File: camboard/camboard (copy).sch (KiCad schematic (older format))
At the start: 7 parts

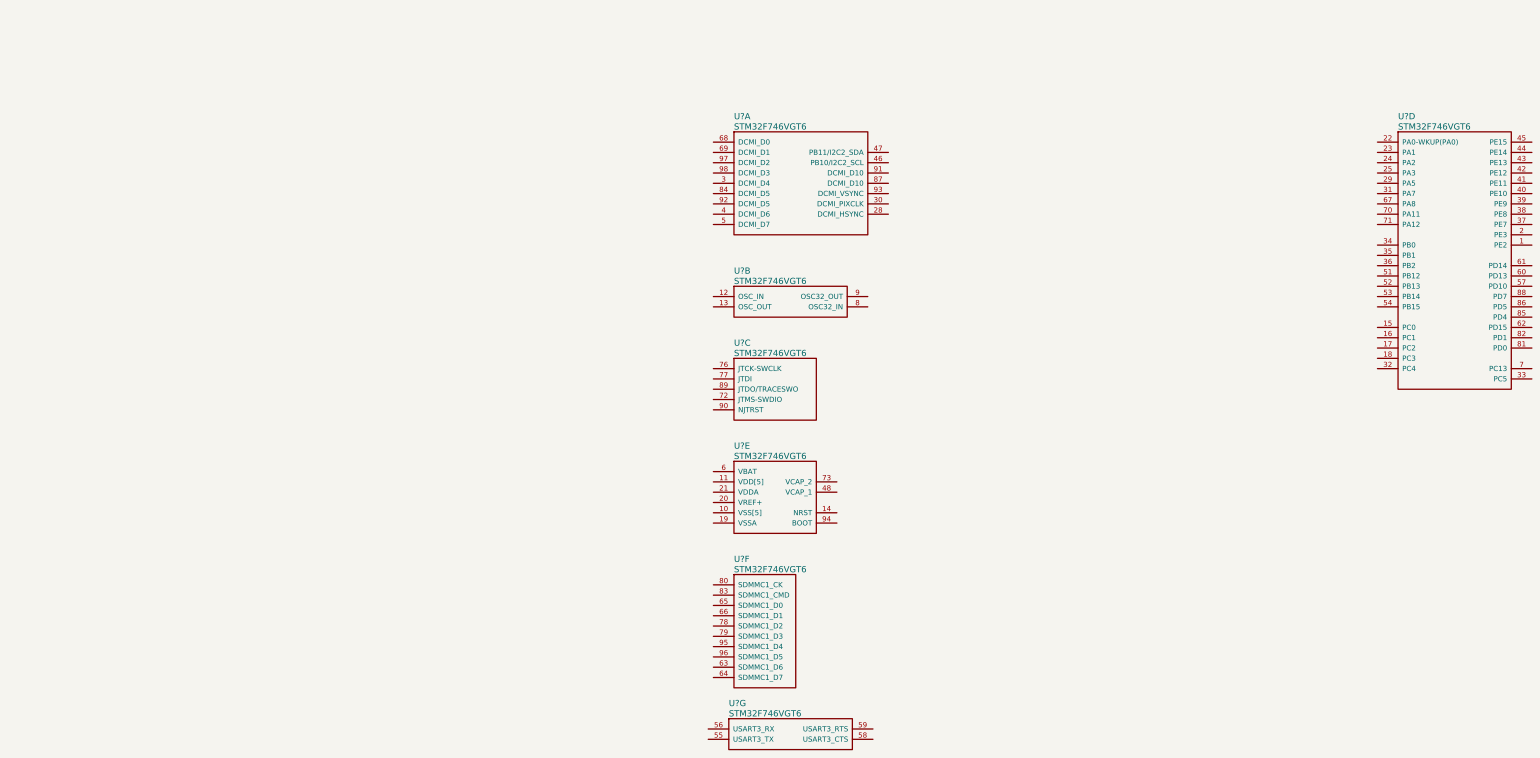
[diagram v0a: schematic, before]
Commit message: Moved components into proper directory
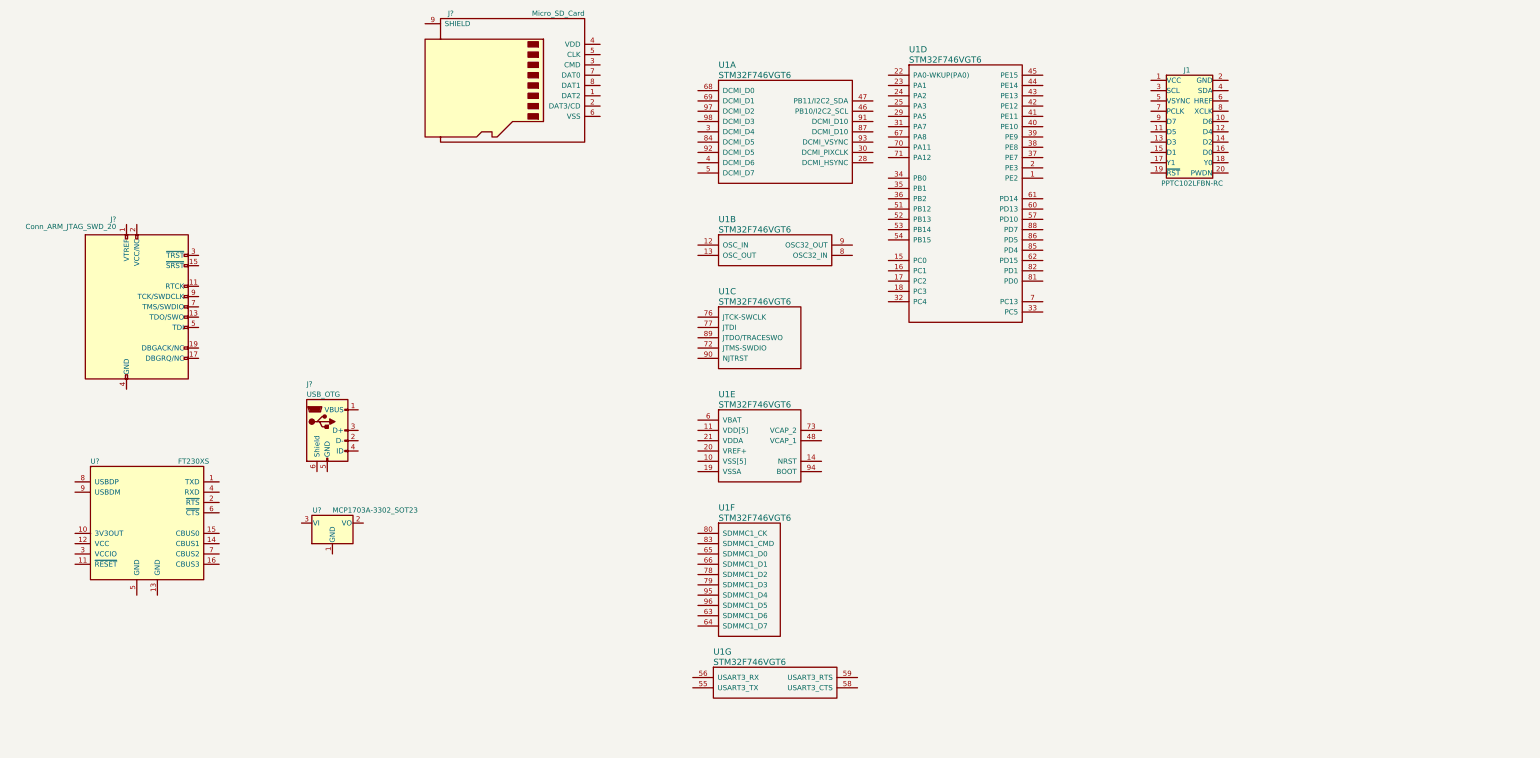
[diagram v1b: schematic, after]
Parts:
- added J1: PPTC102LFBN-RC, symbol PPTC102LFBN-RC
- added J?: Micro_SD_Card, symbol Micro_SD_Card
- added J?: Conn_ARM_JTAG_SWD_20, symbol Conn_ARM_JTAG_SWD_20
- added J?: USB_OTG, symbol USB_OTG
- added U?: FT230XS, SSOP-16, symbol FT230XS
- added U?: MCP1703A-3302_SOT23, TO_SOT_Packages_SMD:SOT-23, symbol MCP1703A-3302_SOT23
- gave numbers to parts that had none: 1
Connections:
- new net GND: J?.10 (GND), J?.12 (GND), J?.14 (GND), J?.16 (GND), J?.18 (GND), J?.20 (GND), J?.4 (GND), J?.6 (GND), J?.8 (GND)
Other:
- moved on the sheet: U1A, U1B, U1C, U1D, U1E, U1F, U1G
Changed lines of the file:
@@
 EESchema Schematic File Version 2
+LIBS:components
+LIBS:connectors
+LIBS:stm32-v2
 LIBS:power
 LIBS:device
@@
 LIBS:contrib
 LIBS:valves
-LIBS:STM32F7x
-LIBS:stm32-v2
-LIBS:camboard-cache
+LIBS:ftdi
+LIBS:camboard (copy)-cache
 EELAYER 25 0
 EELAYER END
@@
 $EndDescr
 $Comp
-L STM32F746VGT6 U?
+L STM32F746VGT6 U1
 U 1 1 59CAFAA7
-P 1300 1750
-F 0 "U?" H 1500 2000 60  0000 L CNN
-F 1 "STM32F746VGT6" H 1500 1900 60  0000 L CNN
-F 2 "" H 1300 1750 60  0001 C CNN
-F 3 "" H 1300 1750 60  0001 C CNN
-	1    1300 1750
+P 1150 1250
+F 0 "U1" H 1350 1500 60  0000 L CNN
+F 1 "STM32F746VGT6" H 1350 1400 60  0000 L CNN
+F 2 "" H 1150 1250 60  0001 C CNN
+F 3 "" H 1150 1250 60  0001 C CNN
+	1    1150 1250
 	1    0    0    -1
 $EndComp
 $Comp
-L STM32F746VGT6 U?
+L STM32F746VGT6 U1
 U 2 1 59CAFB26
-P 1300 3250
-F 0 "U?" H 1500 3500 60  0000 L CNN
-F 1 "STM32F746VGT6" H 1500 3400 60  0000 L CNN
-F 2 "" H 1300 3250 60  0001 C CNN
-F 3 "" H 1300 3250 60  0001 C CNN
-	2    1300 3250
+P 1150 2750
+F 0 "U1" H 1350 3000 60  0000 L CNN
+F 1 "STM32F746VGT6" H 1350 2900 60  0000 L CNN
+F 2 "" H 1150 2750 60  0001 C CNN
+F 3 "" H 1150 2750 60  0001 C CNN
+	2    1150 2750
 	1    0    0    -1
 $EndComp
 $Comp
-L STM32F746VGT6 U?
+L STM32F746VGT6 U1
 U 3 1 59CAFB7D
-P 1300 3950
-F 0 "U?" H 1500 4200 60  0000 L CNN
-F 1 "STM32F746VGT6" H 1500 4100 60  0000 L CNN
-F 2 "" H 1300 3950 60  0001 C CNN
-F 3 "" H 1300 3950 60  0001 C CNN
-	3    1300 3950
+P 1150 3450
+F 0 "U1" H 1350 3700 60  0000 L CNN
+F 1 "STM32F746VGT6" H 1350 3600 60  0000 L CNN
+F 2 "" H 1150 3450 60  0001 C CNN
+F 3 "" H 1150 3450 60  0001 C CNN
+	3    1150 3450
 	1    0    0    -1
 $EndComp
 $Comp
-L STM32F746VGT6 U?
+L STM32F746VGT6 U1
 U 4 1 59CAFBB8
-P 7750 1750
-F 0 "U?" H 7950 2000 60  0000 L CNN
-F 1 "STM32F746VGT6" H 7950 1900 60  0000 L CNN
-F 2 "" H 7750 1750 60  0001 C CNN
-F 3 "" H 7750 1750 60  0001 C CNN
-	4    7750 1750
+P 3000 1100
+F 0 "U1" H 3200 1350 60  0000 L CNN
+F 1 "STM32F746VGT6" H 3200 1250 60  0000 L CNN
+F 2 "" H 3000 1100 60  0001 C CNN
+F 3 "" H 3000 1100 60  0001 C CNN
+	4    3000 1100
 	1    0    0    -1
 $EndComp
 $Comp
-L STM32F746VGT6 U?
+L STM32F746VGT6 U1
 U 5 1 59CAFC81
-P 1300 4950
-F 0 "U?" H 1500 5200 60  0000 L CNN
-F 1 "STM32F746VGT6" H 1500 5100 60  0000 L CNN
-F 2 "" H 1300 4950 60  0001 C CNN
-F 3 "" H 1300 4950 60  0001 C CNN
-	5    1300 4950
+P 1150 4450
+F 0 "U1" H 1350 4700 60  0000 L CNN
+F 1 "STM32F746VGT6" H 1350 4600 60  0000 L CNN
+F 2 "" H 1150 4450 60  0001 C CNN
+F 3 "" H 1150 4450 60  0001 C CNN
+	5    1150 4450
 	1    0    0    -1
 $EndComp
 $Comp
-L STM32F746VGT6 U?
+L STM32F746VGT6 U1
 U 6 1 59CAFD02
-P 1300 6050
-F 0 "U?" H 1500 6300 60  0000 L CNN
-F 1 "STM32F746VGT6" H 1500 6200 60  0000 L CNN
-F 2 "" H 1300 6050 60  0001 C CNN
-F 3 "" H 1300 6050 60  0001 C CNN
-	6    1300 6050
+P 1150 5550
+F 0 "U1" H 1350 5800 60  0000 L CNN
+F 1 "STM32F746VGT6" H 1350 5700 60  0000 L CNN
+F 2 "" H 1150 5550 60  0001 C CNN
+F 3 "" H 1150 5550 60  0001 C CNN
+	6    1150 5550
 	1    0    0    -1
 $EndComp
 $Comp
-L STM32F746VGT6 U?
+L STM32F746VGT6 U1
 U 7 1 59CAFE6F
-P 1250 7450
-F 0 "U?" H 1450 7700 60  0000 L CNN
-F 1 "STM32F746VGT6" H 1450 7600 60  0000 L CNN
-F 2 "" H 1250 7450 60  0001 C CNN
-F 3 "" H 1250 7450 60  0001 C CNN
-	7    1250 7450
+P 1100 6950
+F 0 "U1" H 1300 7200 60  0000 L CNN
+F 1 "STM32F746VGT6" H 1300 7100 60  0000 L CNN
+F 2 "" H 1100 6950 60  0001 C CNN
+F 3 "" H 1100 6950 60  0001 C CNN
+	7    1100 6950
 	1    0    0    -1
 $EndComp
+$Comp
+L PPTC102LFBN-RC J1
+U 1 1 59CBC2A2
+P 5750 1550
+F 0 "J1" H 5900 2050 50  0000 C CNN
+F 1 "PPTC102LFBN-RC" H 5950 950 50  0000 C CNN
+F 2 "" H 4400 1400 50  0001 C CNN
+F 3 "" H 6050 2050 50  0001 C CNN
+	1    5750 1550
+	1    0    0    -1
+$EndComp
+$Comp
+L Micro_SD_Card J?
+U 1 1 59CBC7CA
+P -600 1100
+F 0 "J?" H -1250 1700 50  0000 C CNN
+F 1 "Micro_SD_Card" H 50  1700 50  0000 R CNN
+F 2 "" H 550 1400 50  0001 C CNN
+F 3 "" H -600 1100 50  0001 C CNN
+	1    -600 1100
+	1    0    0    -1
+$EndComp
+$Comp
+L Conn_ARM_JTAG_SWD_20 J?
+U 1 1 59CBC9BD
+P -4300 3350
+F 0 "J?" H -4500 4200 50  0000 R CNN
+F 1 "Conn_ARM_JTAG_SWD_20" H -4500 4100 50  0000 R BNN
+F 2 "" H -3850 2300 50  0001 L TNN
+F 3 "" V -4650 2100 50  0001 C CNN
+	1    -4300 3350
+	1    0    0    -1
+$EndComp
+$Comp
+L FT230XS U?
+U 1 1 59CBCC25
+P -4200 5450
+F 0 "U?" H -4750 6050 50  0000 L CNN
+F 1 "FT230XS" H -3900 6050 50  0000 L CNN
+F 2 "SSOP-16" H -4200 5450 50  0001 C CNN
+F 3 "" H -4200 5450 50  0001 C CNN
+	1    -4200 5450
+	1    0    0    -1
+$EndComp
+$Comp
+L USB_OTG J?
+U 1 1 59CBCF26
+P -2450 4550
+F 0 "J?" H -2650 5000 50  0000 L CNN
+F 1 "USB_OTG" H -2650 4900 50  0000 L CNN
+F 2 "" H -2300 4500 50  0001 C CNN
+F 3 "" H -2300 4500 50  0001 C CNN
+	1    -2450 4550
+	1    0    0    -1
+$EndComp
+$Comp
+L MCP1703A-3302_SOT23 U?
+U 1 1 59CBCF8D
+P -2400 5450
+F 0 "U?" H -2550 5575 50  0000 C CNN
+F 1 "MCP1703A-3302_SOT23" H -2400 5575 50  0000 L CNN
+F 2 "TO_SOT_Packages_SMD:SOT-23" H -2400 5650 50  0001 C CNN
+F 3 "" H -2400 5400 50  0001 C CNN
+	1    -2400 5450
+	1    0    0    -1
+$EndComp

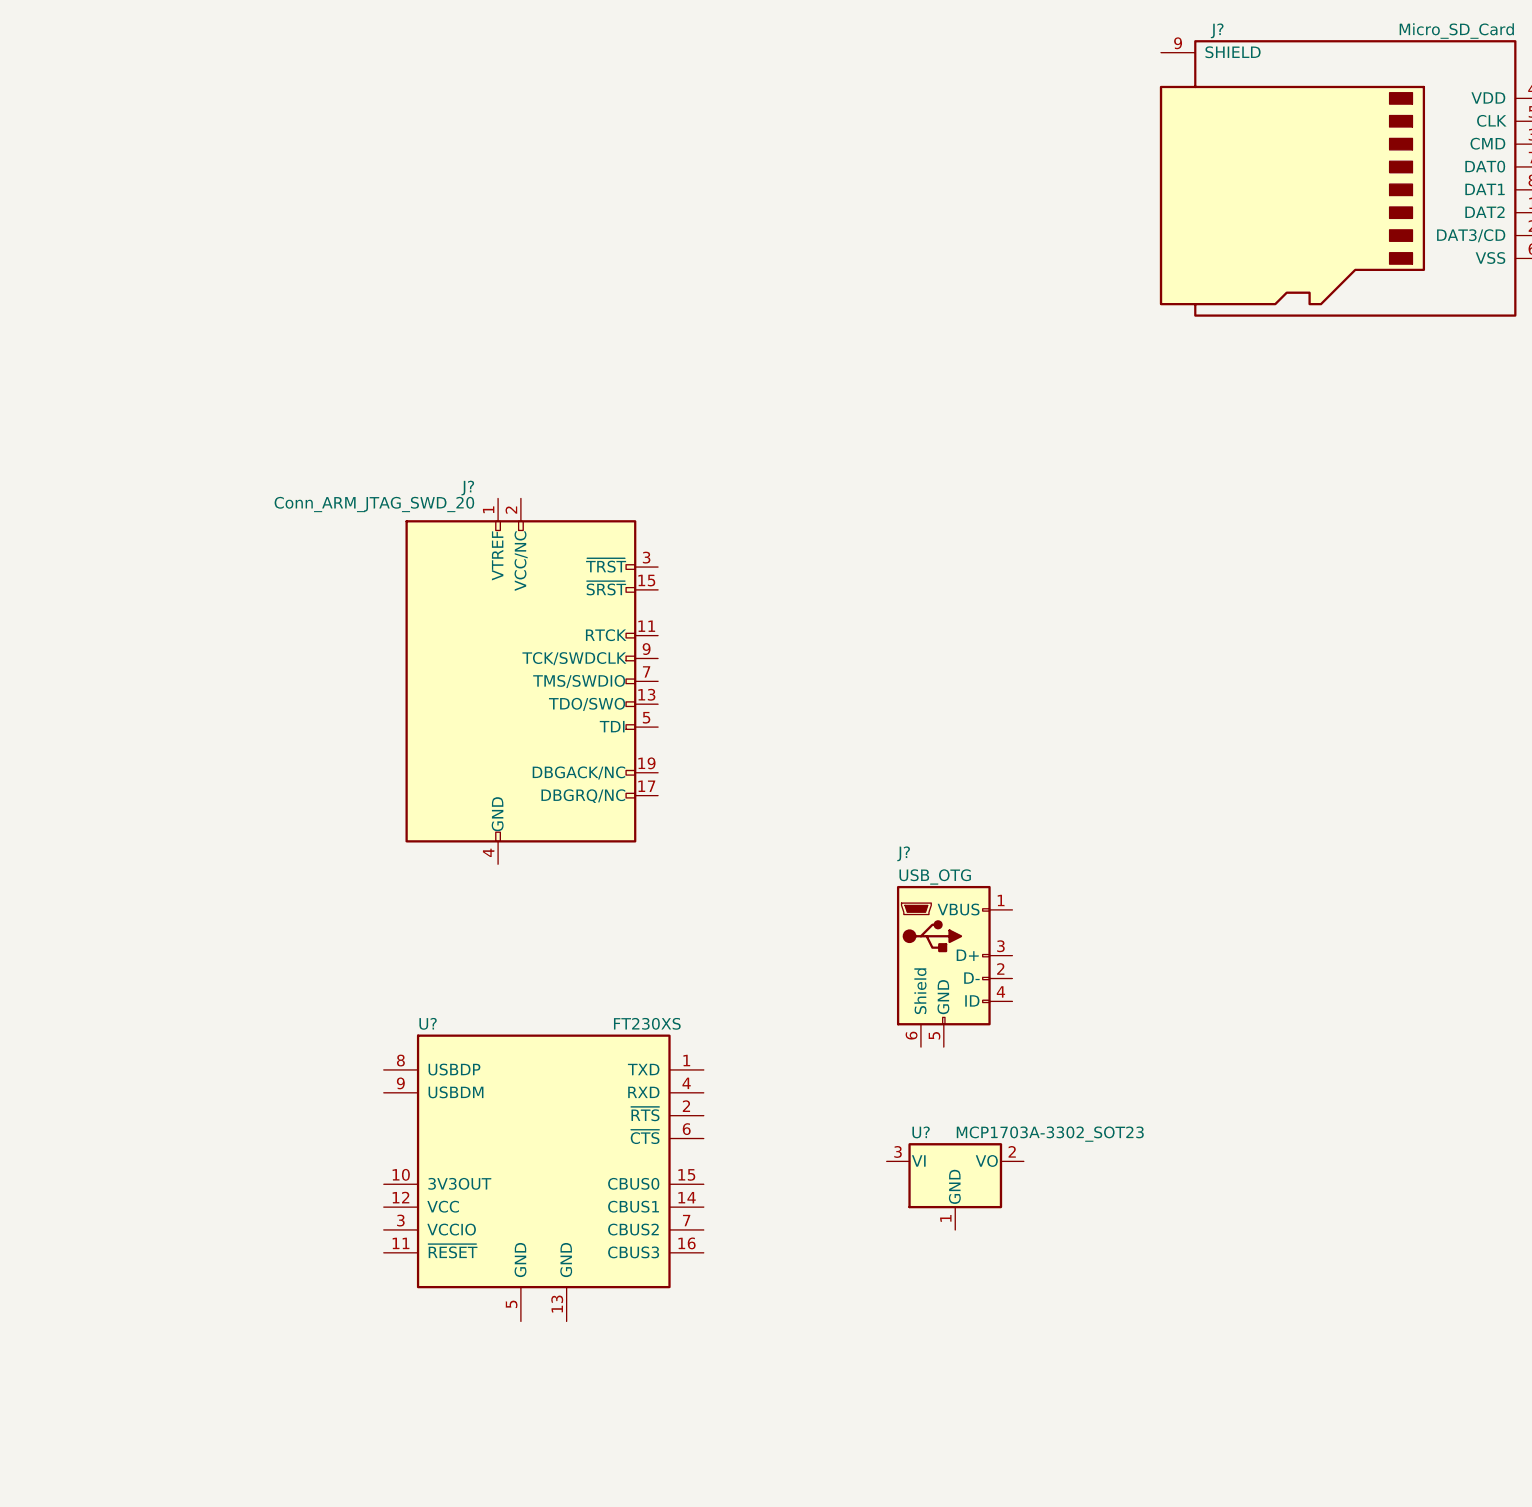
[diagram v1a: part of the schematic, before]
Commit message: Added i2c pins to camera block
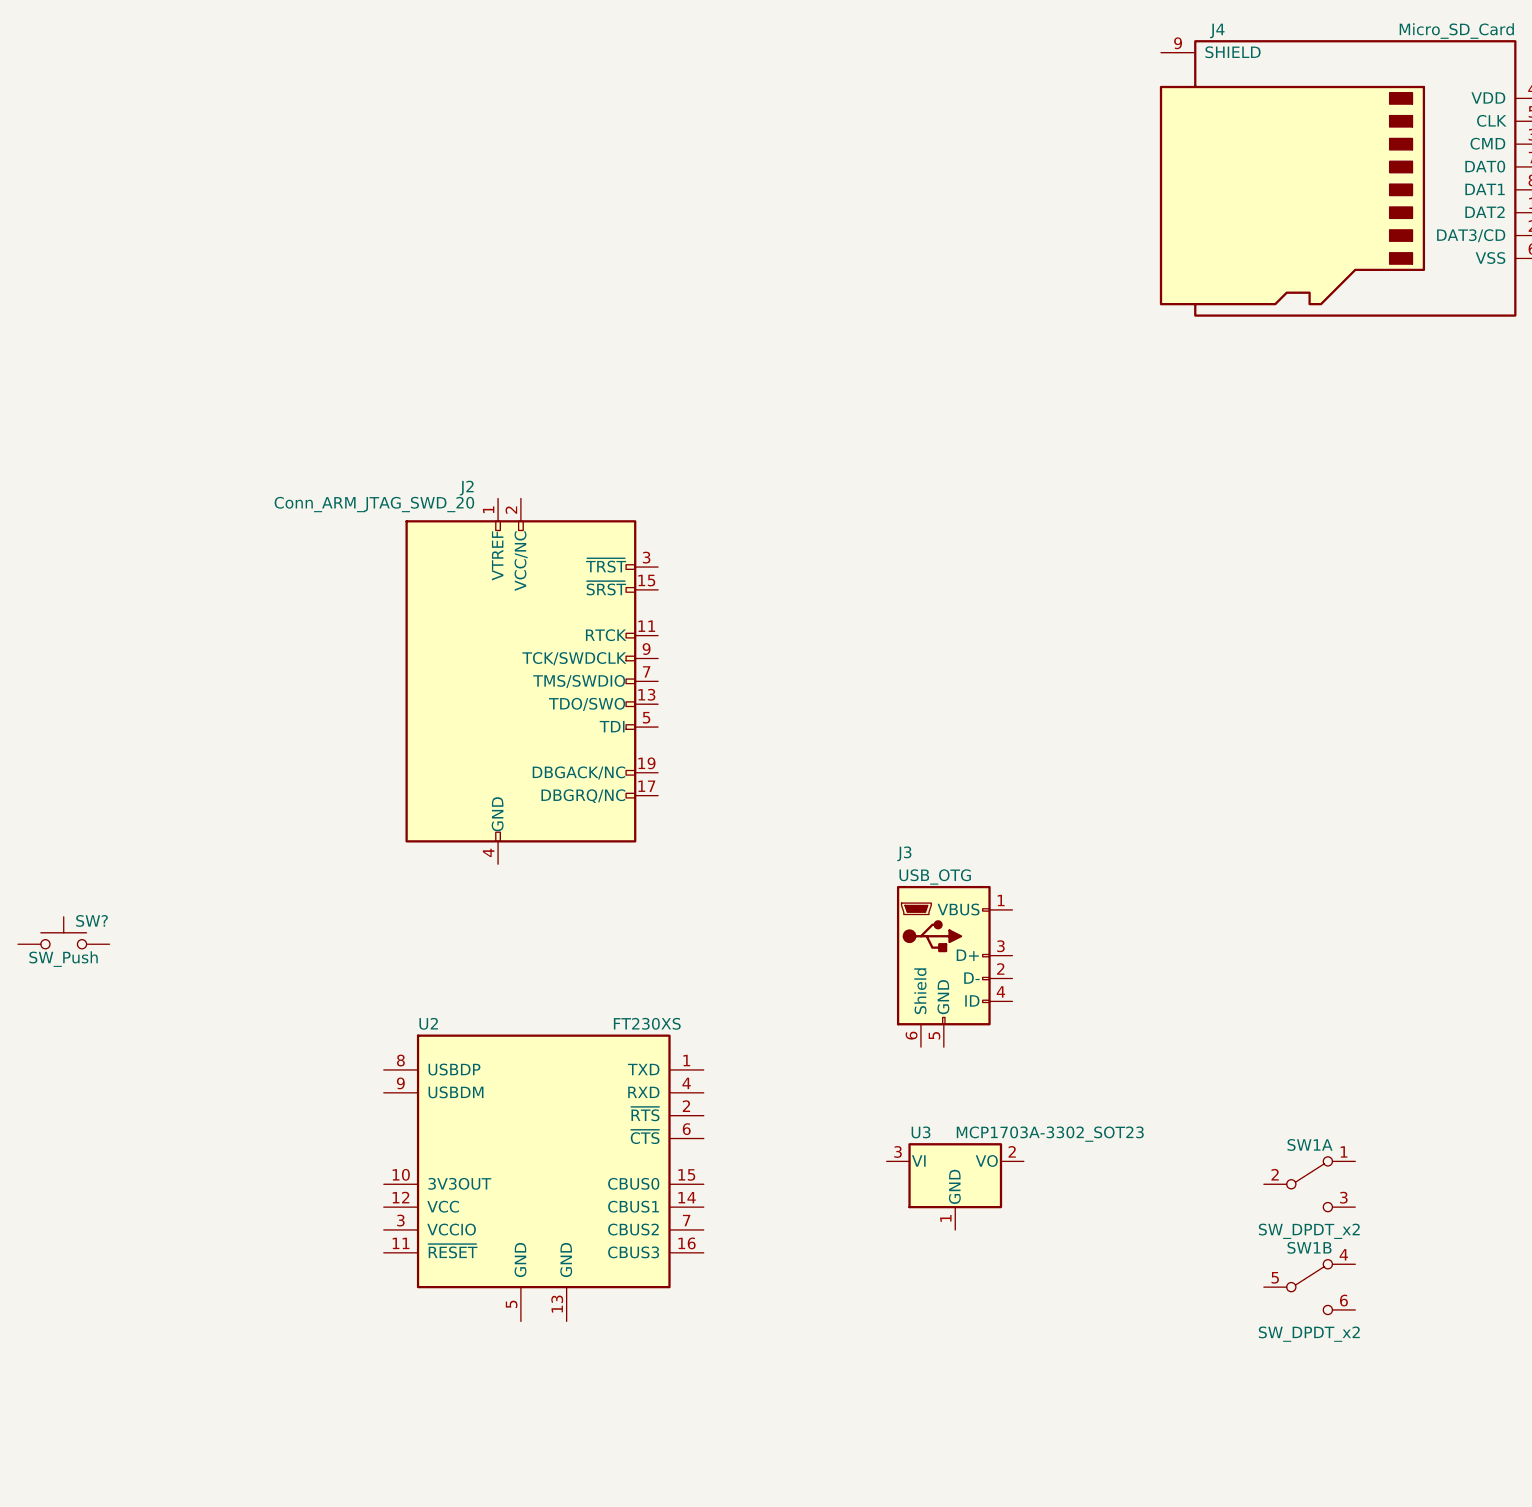
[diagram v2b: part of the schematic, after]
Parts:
- added SW1: SW_DPDT_x2, symbol SW_DPDT_x2
- added SW?: SW_Push, symbol SW_Push
- gave numbers to parts that had none: 5
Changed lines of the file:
@@
 $EndComp
 $Comp
-L Micro_SD_Card J?
+L Micro_SD_Card J4
 U 1 1 59CBC7CA
 P -600 1100
-F 0 "J?" H -1250 1700 50  0000 C CNN
+F 0 "J4" H -1250 1700 50  0000 C CNN
 F 1 "Micro_SD_Card" H 50  1700 50  0000 R CNN
 F 2 "" H 550 1400 50  0001 C CNN
@@
 $EndComp
 $Comp
-L Conn_ARM_JTAG_SWD_20 J?
+L Conn_ARM_JTAG_SWD_20 J2
 U 1 1 59CBC9BD
 P -4300 3350
-F 0 "J?" H -4500 4200 50  0000 R CNN
+F 0 "J2" H -4500 4200 50  0000 R CNN
 F 1 "Conn_ARM_JTAG_SWD_20" H -4500 4100 50  0000 R BNN
 F 2 "" H -3850 2300 50  0001 L TNN
@@
 $EndComp
 $Comp
-L FT230XS U?
+L FT230XS U2
 U 1 1 59CBCC25
 P -4200 5450
-F 0 "U?" H -4750 6050 50  0000 L CNN
+F 0 "U2" H -4750 6050 50  0000 L CNN
 F 1 "FT230XS" H -3900 6050 50  0000 L CNN
 F 2 "SSOP-16" H -4200 5450 50  0001 C CNN
@@
 $EndComp
 $Comp
-L USB_OTG J?
+L USB_OTG J3
 U 1 1 59CBCF26
 P -2450 4550
-F 0 "J?" H -2650 5000 50  0000 L CNN
+F 0 "J3" H -2650 5000 50  0000 L CNN
 F 1 "USB_OTG" H -2650 4900 50  0000 L CNN
 F 2 "" H -2300 4500 50  0001 C CNN
@@
 $EndComp
 $Comp
-L MCP1703A-3302_SOT23 U?
+L MCP1703A-3302_SOT23 U3
 U 1 1 59CBCF8D
 P -2400 5450
-F 0 "U?" H -2550 5575 50  0000 C CNN
+F 0 "U3" H -2550 5575 50  0000 C CNN
 F 1 "MCP1703A-3302_SOT23" H -2400 5575 50  0000 L CNN
 F 2 "TO_SOT_Packages_SMD:SOT-23" H -2400 5650 50  0001 C CNN
@@
 	1    0    0    -1
 $EndComp
+$Comp
+L SW_DPDT_x2 SW1
+U 1 1 59CBC0C9
+P -850 5550
+F 0 "SW1" H -850 5720 50  0000 C CNN
+F 1 "SW_DPDT_x2" H -850 5350 50  0000 C CNN
+F 2 "" H -850 5550 50  0001 C CNN
+F 3 "" H -850 5550 50  0001 C CNN
+	1    -850 5550
+	1    0    0    -1
+$EndComp
+$Comp
+L SW_DPDT_x2 SW1
+U 2 1 59CBC161
+P -850 6000
+F 0 "SW1" H -850 6170 50  0000 C CNN
+F 1 "SW_DPDT_x2" H -850 5800 50  0000 C CNN
+F 2 "" H -850 6000 50  0001 C CNN
+F 3 "" H -850 6000 50  0001 C CNN
+	2    -850 6000
+	1    0    0    -1
+$EndComp
+$Comp
+L SW_Push SW?
+U 1 1 59CBC9F2
+P -6300 4500
+F 0 "SW?" H -6250 4600 50  0000 L CNN
+F 1 "SW_Push" H -6300 4440 50  0000 C CNN
+F 2 "" H -6300 4700 50  0001 C CNN
+F 3 "" H -6300 4700 50  0001 C CNN
+	1    -6300 4500
+	1    0    0    -1
+$EndComp
